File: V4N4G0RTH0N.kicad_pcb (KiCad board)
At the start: 2 copper layers, 242.9 x 96.6 mm, 125 parts, among them U1 ATmega32U4-A, U2 SRV05-4, Y1 16MHz

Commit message: V4N v2
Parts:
- added C8: 4.7n, Capacitor_SMD:C_0805_2012Metric, B.Cu at (60.6, 31.0)
- added R10: 1M, Resistor_SMD:R_0805_2012Metric, B.Cu at (58.5, 31.0)
- added R3: 10k, Resistor_SMD:R_0805_2012Metric, B.Cu at (127.6, 115.4)
- moved R9 5.08 mm to (64.5, 29.7)
- moved R4 4.42 mm to (151.6, 104.6), turned to 180 degrees
- moved C7 1.55 mm to (152.7, 107.2), turned to 0 degrees
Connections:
- USB1 pad 13: GND -> Earth
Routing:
- net GND: track 295.6 -> 265.4 mm, vias 10 -> 8
- net +5V: track 212.7 -> 239.2 mm
- net Earth: track 0.00 -> 22.3 mm
- net Net-(R9-Pad2): track 8.20 -> 12.8 mm
- net Net-(R4-Pad2): track 7.10 -> 3.70 mm
- net Net-(D54-Pad2): track 24.9 -> 27.8 mm
- added copper zone on F.Cu, net GND

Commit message: Add slider
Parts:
- removed G***: LOGO, SILK:ORTHOVAN3
- added RV1: R_Potentiometer, Potentiometer_THT:Potentiometer_Bourns_PTA3043_Single_Slide, F.Cu at (143.7, 97.6)
- renumbered RESET to D54
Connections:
- U1 pad 41: COL11 -> ANAL_IN
- U1 pad 8: Net-(U1-Pad8) -> COL11
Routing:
- net +5V: track 239.2 -> 298.7 mm, vias 8 -> 10
- net ANAL_IN: track 0.00 -> 30.9 mm, vias 0 -> 2
- net COL11: track 162.7 -> 179.7 mm, vias 1 -> 5
- net COL5: track 115.1 -> 110.8 mm, vias 3 -> 2
- net ROW2: track 248.8 -> 252.0 mm
- net LED_1: track 186.0 -> 189.1 mm
- net LED_3: track 173.3 -> 175.7 mm
- net LED_2: track 180.6 -> 182.4 mm
- net ROW0: track 162.4 -> 163.1 mm

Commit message: still need to do some cleanup
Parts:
- moved RV1 0.16 mm to (143.5, 97.6)
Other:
- board text removed: "ORTHO GOOD"
- board text removed: "STAGGER BAD"

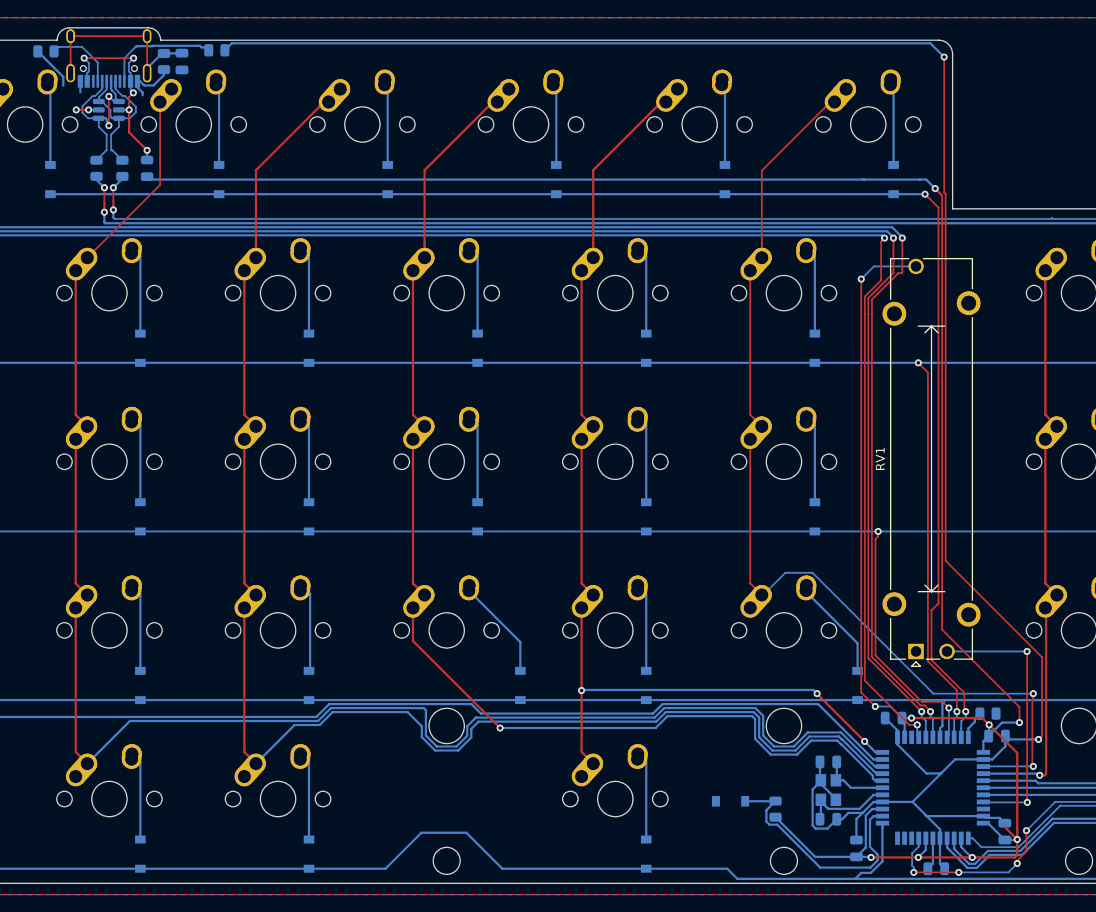
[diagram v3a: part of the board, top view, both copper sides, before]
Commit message: Update pcb to remove nub for v3 compatibility
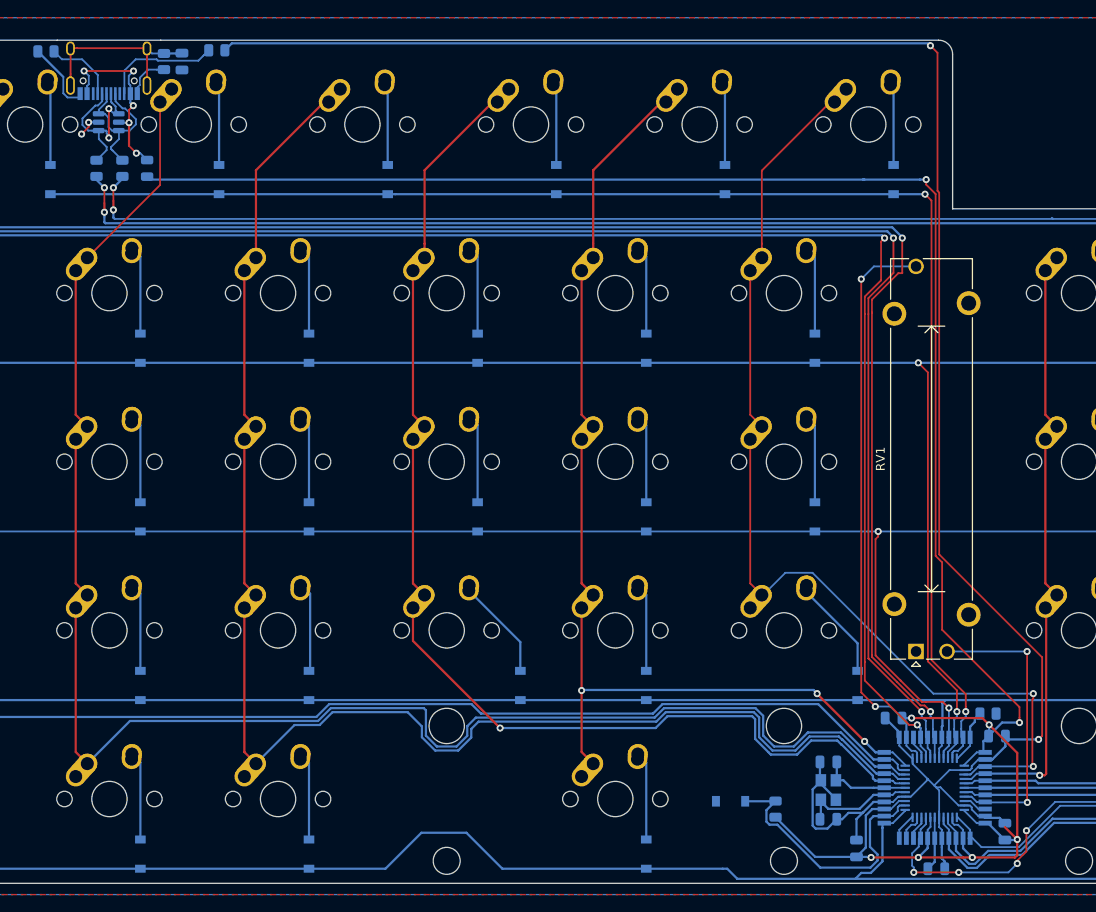
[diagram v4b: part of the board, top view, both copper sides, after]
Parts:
- U1: footprint Package_QFP:TQFP-44_10x10mm_P0.8mm -> s8erdude-keyboard-parts:QFN_TQFP-44_Combined
- moved U2 1.39 mm to (52.3, 37.8)
- moved USB1 1.39 mm to (52.3, 26.9)
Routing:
- net +5V: track 298.7 -> 316.6 mm
- net Net-(U1-Pad10): track 0.00 -> 3.11 mm
- net COL0: track 191.0 -> 194.1 mm
- net Net-(D54-Pad2): track 27.8 -> 30.9 mm
- net Net-(U1-Pad11): track 0.00 -> 3.04 mm
- net ROW4: track 239.3 -> 242.4 mm
- net COL7: track 87.1 -> 90.1 mm
- net COL4: track 112.6 -> 115.7 mm
- net COL5: track 110.8 -> 113.5 mm
- net GND: track 265.7 -> 268.5 mm
- net ROW1: track 267.8 -> 270.6 mm
- net Net-(U1-Pad9): track 0.00 -> 2.74 mm
- net Net-(U1-Pad25): track 0.00 -> 2.74 mm
- net Net-(U1-Pad42): track 0.00 -> 2.74 mm
- net COL1: track 179.6 -> 182.3 mm
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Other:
- board size 242.9 x 96.6 mm -> 242.9 x 95.2 mm
